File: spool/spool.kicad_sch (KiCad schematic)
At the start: 157 parts, among them J1 USB_B_Micro, J13 Conn_02x10_Counter_Clockwise, J1901 TC2030, J2 SWD, J3 Conn_01x03, J4 Switch_1, J5 Conn_01x03, J6 Switch_2, J8 Conn_01x08, J9 Switch_2, M1 Motor_DC, M2 Servo, M3 Servo, Q1 AO3400A, Q101 Q_NMOS_GSD, Q2 2N7002, SW1 USB_BOOT, SW2 RESET, SW4 SW_Coded_SH-7010, SW5 SW_Push_DPDT, U1 TPS63070RNMR, U10 HT75xx-1-SOT89, U102 INA219AxDCN, U103 DY-ITR8402, U104 DY-ITR8402, U106 M24C02-WMN, U14 PCF8563T, U2 PA_PIR, U3 AS5600-ASOT, U6 DRV8871DDA, U7 W25Q128JVS, U8 RP2040, U9 LMR14050S, Y1 Crystal_GND24, Y2 Crystal

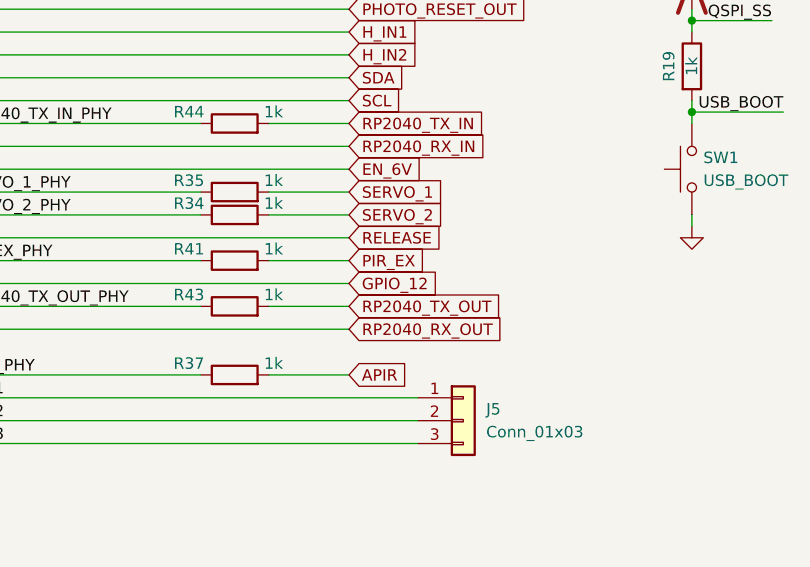
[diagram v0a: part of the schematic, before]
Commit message: Fix pin label
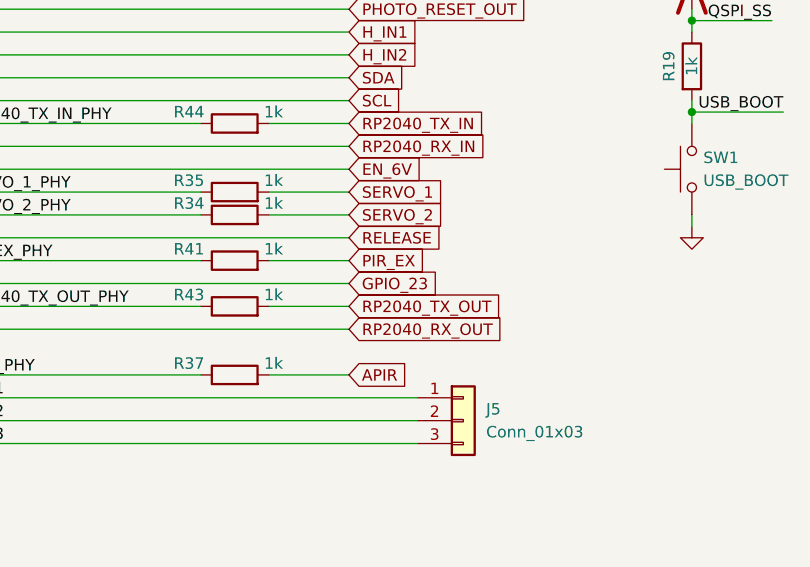
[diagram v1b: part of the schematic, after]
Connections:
- net GPIO_12: no longer U8.35 (GPIO23)
- new net GPIO_23: U8.35 (GPIO23)
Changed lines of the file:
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@@
 		)
 	)
-	(global_label "GPIO_12"
+	(global_label "GPIO_23"
 		(shape input)
 		(at 523.24 125.73 0)

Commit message: Adding STM32 version
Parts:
- removed C11, C12, C13, C14, C15, C16, C17, C18, C19: 100nF, Capacitor_SMD:C_0402_1005Metric, symbol Device:C
- removed C20, C21: 1uF, Capacitor_SMD:C_0402_1005Metric, symbol Device:C
- removed J1: USB_B_Micro, cacophony-library:MICRO-USB-TH_MICRO-USB-A14, symbol Connector:USB_B_Micro
- removed J3: Conn_01x03, Connector_JST:JST_SH_BM03B-SRSS-TB_1x03-1MP_P1.00mm_Vertical, symbol Connector_Generic_MountingPin:Conn_01x03_MountingPin
- removed J4: Switch_1, Connector_JST:JST_SH_BM02B-SRSS-TB_1x02-1MP_P1.00mm_Vertical, symbol Connector_Generic_MountingPin:Conn_01x02_MountingPin
- removed J5: Conn_01x03, Connector_PinHeader_2.54mm:PinHeader_1x03_P2.54mm_Vertical, symbol Connector_Generic:Conn_01x03
- removed J6: Switch_2, Connector_JST:JST_SH_BM02B-SRSS-TB_1x02-1MP_P1.00mm_Vertical, symbol Connector_Generic_MountingPin:Conn_01x02_MountingPin
- removed J8: Conn_01x08, Connector_JST:JST_XA_S08B-XASK-1_1x08_P2.50mm_Horizontal, symbol Connector_Generic:Conn_01x08
- removed M2, M3: Servo, Connector_JST:JST_XA_B03B-XASK-1-A_1x03_P2.50mm_Vertical, symbol cacophony-library:Servo
- removed R16, R17: 33ohm, Resistor_SMD:R_0402_1005Metric, symbol Device:R
- removed R18: DNF, Resistor_SMD:R_0402_1005Metric, symbol Device:R
- removed R43: 1k, Resistor_SMD:R_0402_1005Metric, symbol Device:R
- removed U7: W25Q128JVS, Package_SO:SOIC-8_5.3x5.3mm_P1.27mm, symbol Memory_Flash:W25Q128JVS
- removed U8: RP2040, cacophony-library:RP2040-QFN-56, symbol cacophony-library:RP2040
- removed Y1: Crystal_GND24, Crystal:Crystal_SMD_3225-4Pin_3.2x2.5mm, symbol Device:Crystal_GND24
- added C41, C51: 100nF, Capacitor_SMD:C_0402_1005Metric, symbol Device:C
- added C42, C43, C44, C45: 100nF, Capacitor_SMD:C_0402_1005Metric, symbol Device:C_Small
- added D204: D_Zener, Diode_SMD:D_SOD-123, symbol Device:D_Zener
- added H14: MountingHole, cacophony-library:MountingHole_3.5mm_M3, symbol Mechanical:MountingHole
- added H16, H17: KeyHole, cacophony-library:3.0mm_key_hole, symbol Mechanical:MountingHole
- added J1, J3: Conn_01x04, Connector_PinHeader_2.54mm:PinHeader_1x04_P2.54mm_Vertical, symbol Connector_Generic:Conn_01x04
- added J14: Conn_02x10_Counter_Clockwise, Connector_PinSocket_2.54mm:PinSocket_2x10_P2.54mm_Vertical, symbol Connector_Generic:Conn_02x10_Odd_Even
- added R201: 3.3M, Resistor_SMD:R_0603_1608Metric, symbol Device:R
- added R202: 1M, Resistor_SMD:R_0603_1608Metric, symbol Device:R
- added R24, R28, R5: 10k, Resistor_SMD:R_0402_1005Metric, symbol Device:R
- added R36, R49, R50: 1k, Resistor_SMD:R_0402_1005Metric, symbol Device:R
- added U5: MCP6001-OT, Package_TO_SOT_SMD:SOT-23-5, symbol Amplifier_Operational:MCP6001-OT
- added U8: STM32L073RZTx, Package_QFP:LQFP-64_10x10mm_P0.5mm, symbol MCU_ST_STM32L0:STM32L073RZTx
- C23, C24: value 12pF -> 100nF; LCSC Part C1547 -> C307331
- H11, H12, H13, H5, H6, H7, H8: value MountingHole -> KeyHole
- SW1: value USB_BOOT -> BOOT0
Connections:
- net SERVO_2 is gone; now on net SERVO_2_PHY: R34.2
- net +12V: now also J14.1 (Pin_1), J14.4 (Pin_4)
- net +3V3: now also C23.1, C24.1, SW1.1, C42.1, C43.1, C44.1, C51.1, R24.1, R28.1, U5.5 (V+), U8.1 (VLCD), U8.13 (VDDA), U8.19 (VDD), U8.32 (VDD), U8.48 (VDD_USB), U8.64 (VDD)
- net +6V: now also J14.2 (Pin_2), J14.3 (Pin_3)
- net APIR_PHY: now also U8.14 (PA0)
- net BUZZER: now also U8.30 (PB11)
- net EN_6V: now also U8.61 (PB8)
- net EN_PHOTO_PHY: now also R36.1, U8.41 (PA8); no longer D6.2 (A)
- net EX_PIR_POWER: now also J14.16 (Pin_16)
- net GND: now also C23.2, C24.2, C41.2, C42.2, C43.2, C44.2, C45.2, C51.2, D204.2 (A), J14.17 (Pin_17), J14.18 (Pin_18), J14.5 (Pin_5), J14.6 (Pin_6), R202.2, R5.2, U5.2 (V-), U8.12 (VSSA), U8.18 (VSS), U8.31 (VSS), U8.47 (VSS), U8.63 (VSS); no longer C23.1, C24.1, SW1.1
- net H_IN1: now also U8.53 (PC12)
- net H_IN2: now also U8.54 (PD2)
- net NIGHT_ONLY: now also U8.29 (PB10)
- net PHOTO_HOME_OUT: now also U8.51 (PC10)
- net PHOTO_RESET_OUT: now also U8.52 (PC11)
- net PIR_EX: now also J14.12 (Pin_12)
- net PIR_EX_PHY: now also U8.15 (PA1)
- net RELEASE: now also U8.56 (PB4)
- net RUN: now also C41.1, U8.7 (NRST)
- net R_ENC_1: now also U8.25 (PC5)
- net R_ENC_2: now also U8.27 (PB1)
- net R_ENC_4: now also U8.26 (PB0)
- net R_ENC_8: now also U8.28 (PB2)
- net SCL: now also R28.2, U8.58 (PB6)
- net SDA: now also R24.2, U8.59 (PB7)
- net SERVO_1_PHY: now also U8.23 (PA7)
- net SERVO_2_PHY: now also U8.22 (PA6); no longer R34.1
- net SPOOL_REED_PHY: now also U8.55 (PB3)
- net SWCLK: now also U8.49 (PA14)
- net SWD: now also U8.46 (PA13)
- net SWITCH_1: now also J14.10 (Pin_10)
- net SWITCH_2: now also J14.9 (Pin_9)
- net SW_1_PHY: now also U8.21 (PA5)
- net SW_2_PHY: now also U8.24 (PC4)
- net USB_PHY_D+: now also U8.45 (PA12)
- net USB_PHY_D-: now also U8.44 (PA11)
- net GPIO_12: no longer names the net of J13.4 (Pin_4)
- net QSPI_SS renamed BOOT0
- net BOOT0: now also R5.1, U8.60 (BOOT0)
- net RP2040_TX_IN renamed TX_STM32
- net TX_STM32: now also J14.20 (Pin_20)
- net RP2040_TX_IN_PHY renamed TX_PHY
- net TX_PHY: now also U8.16 (PA2)
- net SERVO_1 renamed SERVO_SIG_1
- net SERVO_SIG_1: now also J14.7 (Pin_7)
- new net: R201.2, R202.1, U5.3 (+)
- new net: D6.2 (A), R36.2
- new net BAT_DIV: R50.2, U5.1, U5.4 (-)
- new net BAT_DIV_PHY: C45.1, R50.1, U8.20 (PA4)
- new net BAT_SENSE: D204.1 (K), J14.15 (Pin_15), R201.1
- new net PB12: J1.1 (Pin_1), U8.33 (PB12)
- new net PB13: J1.2 (Pin_2), U8.34 (PB13)
- new net PB14: J1.3 (Pin_3), U8.35 (PB14)
- new net PB15: J1.4 (Pin_4), U8.36 (PB15)
- new net PC6: J3.4 (Pin_4), U8.37 (PC6)
- new net PC7: J3.3 (Pin_3), U8.38 (PC7)
- new net PC8: J3.2 (Pin_2), U8.39 (PC8)
- new net PC9: J3.1 (Pin_1), U8.40 (PC9)
- new net RX_PHY: R49.1, U8.17 (PA3)
- new net RX_STM32: J14.19 (Pin_19), R49.2
- new net SERVO_SIG_2: J14.8 (Pin_8), R34.1
- new net USART_1_RX: U8.43 (PA10)
- new net USART_1_TX: U8.42 (PA9)
- no-connect marks 27 -> 42
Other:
- note added: "U8: STM32L073RZT6, replaces the RP2040. Pin map: spool-rust docs/PORTING_NOTES.md s5. R5: BOOT0 pull-down. SW1 + R19 pull BOOT0 to +3V3 for the ROM bootloader (USB DFU on PA11/PA12, UART on PA2/PA3). C41: NRST filter cap. PC14/PC15 free for an optional 32.768k crystal. TODO: LCSC part number for U8."
- note removed: "Make sure C21 is close to pin 44 of RP2040"
- note removed: "Make sure R3 and R4 are close to RP2040"
- note removed: "Power/Data plug"
- note removed: "RP2040"
- note removed: "Using 4 1k 0402 resistors to increase the wattage so we don't need a different component."
- moved on the sheet: C22, C27, C28, C29, C40, D6, H10, H7, H8, H9, J2, J9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

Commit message: Add JLCPCB part number
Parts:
- U8: LCSC Part (none) -> C77160
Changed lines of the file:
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@@
 			)
 		)
-		(property "LCSC Part" ""
+		(property "LCSC Part" "C77160"
 			(at 430.53 97.79 0)
 			(hide yes)

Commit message: Update switch JLCPCB part
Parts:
- SW4: LCSC Part C440495 -> C51025675
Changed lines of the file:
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@@
 			)
 		)
-		(property "LCSC Part" "C440495"
+		(property "LCSC Part" "C51025675"
 			(at 25.4 41.91 0)
 			(hide yes)
